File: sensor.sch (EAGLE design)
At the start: 30 parts, among them IC1 TP4056, U1 NX1117C33Z, U3 BMP180, U4 TSL2561, Y1 12mhz

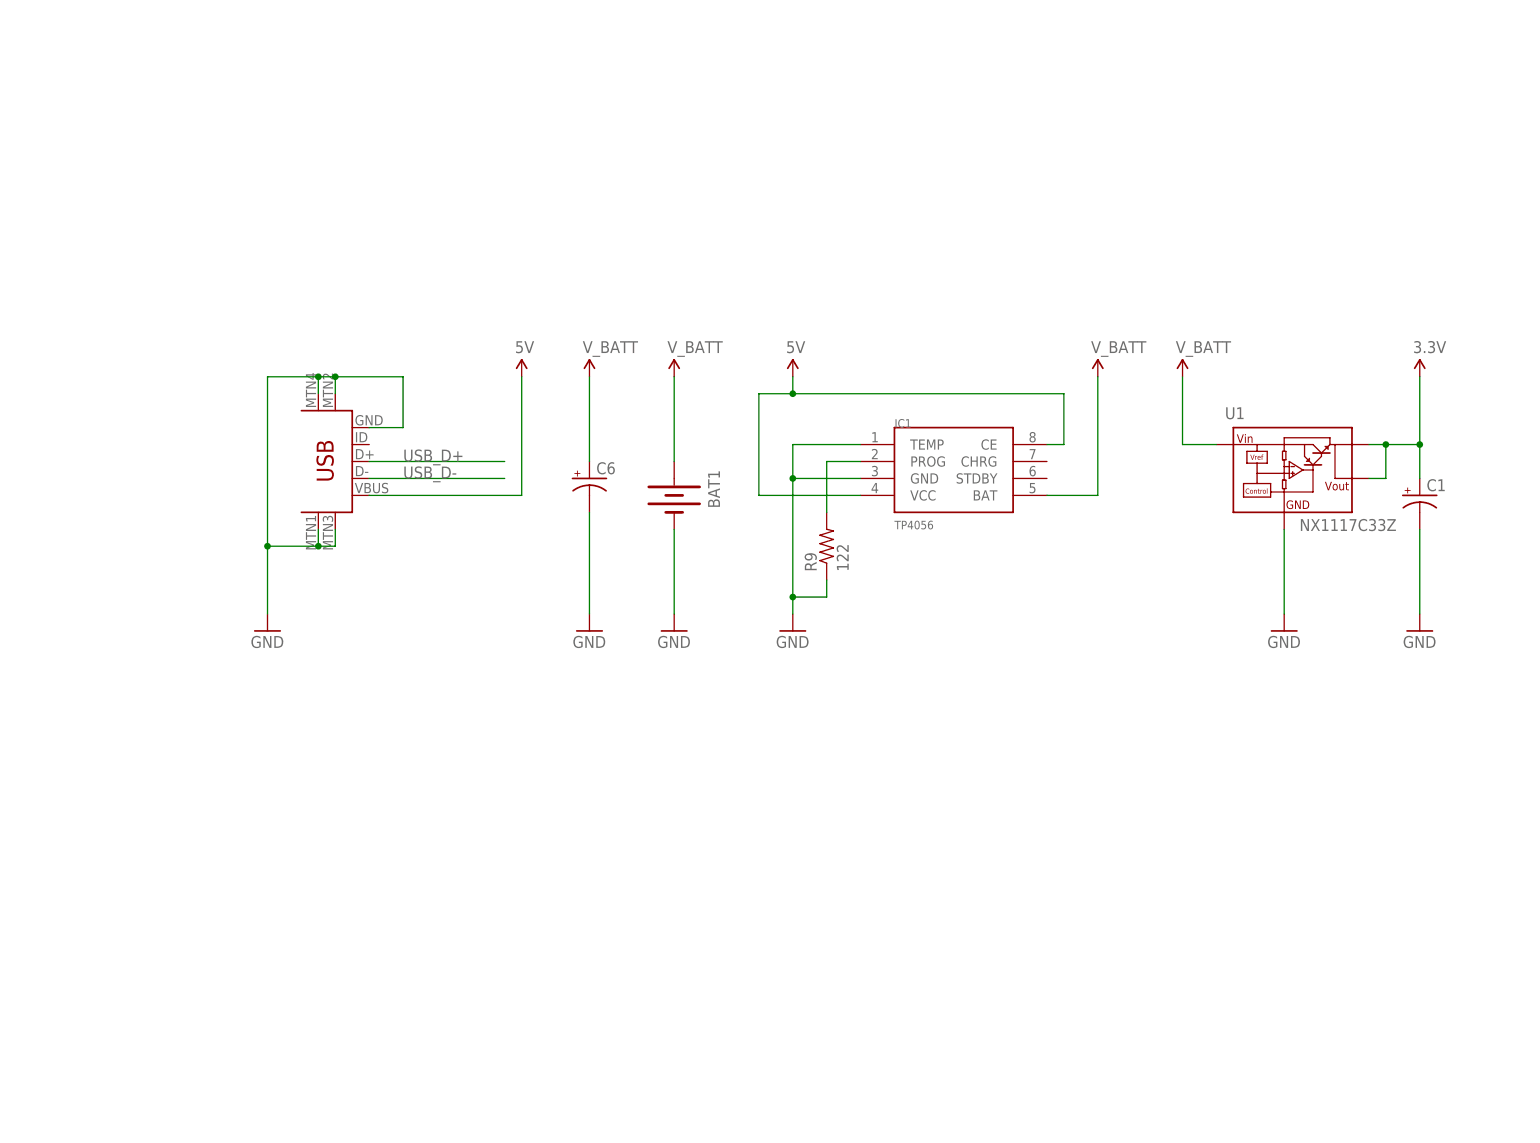
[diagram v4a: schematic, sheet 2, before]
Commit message: Moving to using MCP7381 and TPS63001.. Damn tiny ass packages.
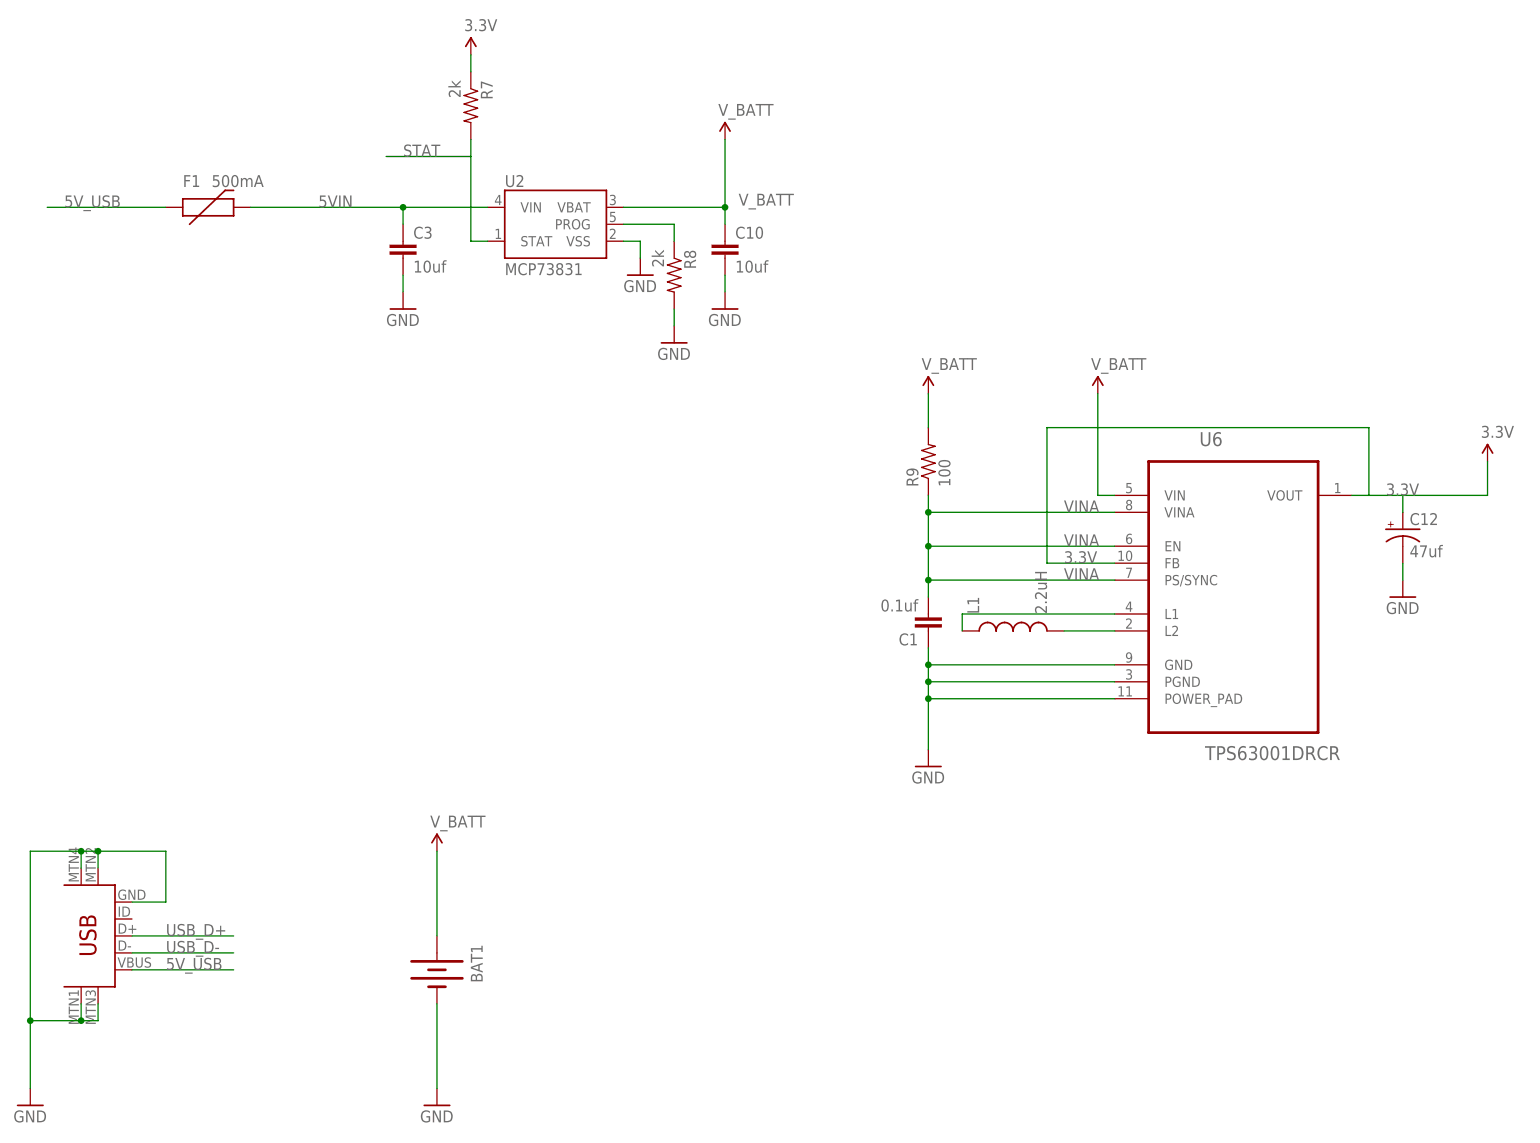
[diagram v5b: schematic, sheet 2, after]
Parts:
- removed C6: (no value), SparkFun-Capacitors:47UF-50V-20%(ELECT)
- removed IC1: TP4056, TP4056:TP4056
- removed U1: NX1117C33Z, nxp_60:NX1117C33Z
- added C10, C3: 10uf, SparkFun-Capacitors:CAP0805
- added C12: 47uf, SparkFun-Capacitors:CAP_POLC
- added EXP_I2C, EXP_UART: (no value), SparkFun-Connectors:M04LOCK
- added F1: 500mA, SparkFun:PTCSMD
- added L1: 2.2uH, SparkFun-Passives:INDUCTORSRU5028
- added R7, R8: 2k, SparkFun-Resistors:RESISTOR0805-RES
- added U2: MCP73831, SparkFun:MCP73831
- added U6: TPS63001DRCR, Texas Instruments_By_element14_Batch_1:TPS63001DRCR
- C1: value (none) -> 0.1uf; device SparkFun-Capacitors:47UF-50V-20%(ELECT) -> SparkFun-Capacitors:CAP0805
- R9: value 122 -> 100
- U$5: value ESP8266_ESP-12 -> (none); device ESP8266-ESP12:ESP8266_ESP-12 -> ESP8266-ESP12E:ESP8266-12EESP8266-ESP12E
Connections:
- net GPIO0 renamed SWITCH
- net GPIO14 renamed LED_R
- net GPIO2 renamed SENSE
- removed net 5V: IC1.CE, IC1.VCC, U$6.VBUS
- removed net GPIO12: LED2.BLU-A, U$5.GPIO12
- removed net GPIO13: U$5.GPIO13
- removed net GPIO16: LED2.GRN-A, U$5.GPIO16
- removed net N$3: IC1.PROG, R9.2
- new net 5VIN: C3.1, F1.2, U2.VIN
- new net 5V_USB: F1.1, U$6.VBUS
- new net LED_B: LED2.BLU-A, U$5.GPIO16
- new net LED_G: LED2.GRN-A, U$5.GPIO12
- new net N$1: L1.2, U6.L2
- new net N$11: R8.1, U2.PROG
- new net N$2: L1.1, U6.L1
- new net SOFT_RX: EXP_UART.2, U$5.GPIO10
- new net SOFT_TX: EXP_UART.1, U$5.GPIO9
- new net STAT: R7.2, U$5.GPIO13, U2.STAT
- new net VINA: C1.2, R9.1, U6.EN, U6.PS/SYNC, U6.VINA
- net 3.3V: now also C12.+, EXP_I2C.4, EXP_UART.4, R7.1, U6.FB, U6.VOUT; no longer C1.+, U1.VOUT, U1.VOUT1
- net GND: now also C1.1, C10.2, C12.-, C3.2, EXP_I2C.3, EXP_UART.3, R8.2, U2.VSS, U6.GND, U6.PGND, U6.POWER_PAD; no longer C1.-, C6.-, IC1.GND, IC1.TEMP, R9.1, U1.GND
- net SCL: now also EXP_I2C.1, U$5.GPIO4; no longer U$5.GPIO5
- net SDA: now also EXP_I2C.2, U$5.GPIO5; no longer U$5.GPIO4
- net V_BATT: now also C10.1, R9.2, U2.VBAT, U6.VIN; no longer C6.+, IC1.BAT, U1.VIN
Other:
- moved on the sheet: BAT1, R9

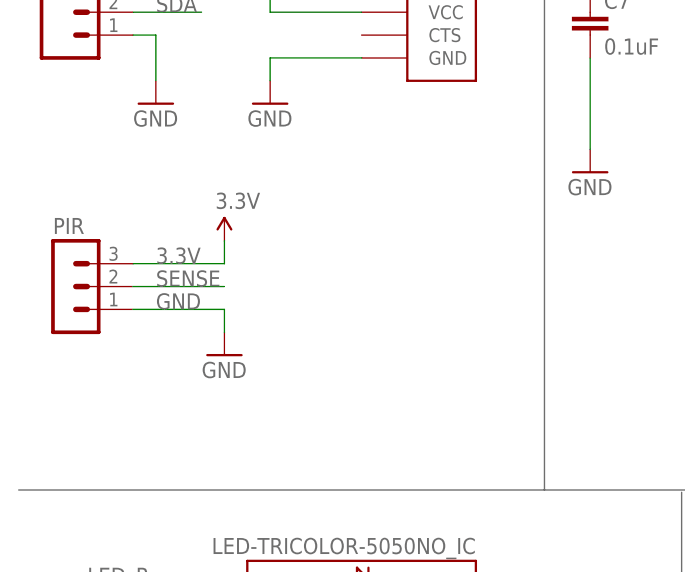
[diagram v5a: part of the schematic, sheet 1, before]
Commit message: Tart the PCB up a bit, nice 45 degree bends. Add a 0.1uf cap across the PIR sensor.
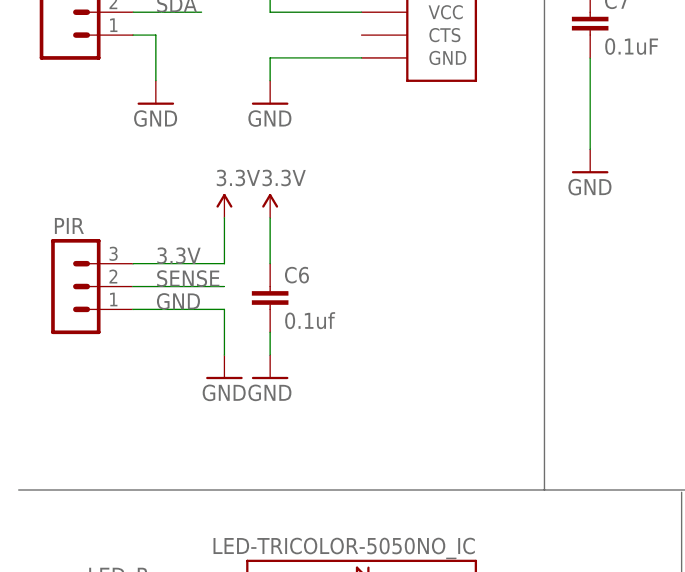
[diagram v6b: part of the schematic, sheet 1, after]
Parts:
- added C6: 0.1uf, SparkFun-Capacitors:CAP0805
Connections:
- net 3.3V: now also C6.1
- net GND: now also C6.2
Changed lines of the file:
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@@
 <part name="EXP_UART" library="SparkFun-Connectors" deviceset="M04" device="LOCK"/>
 <part name="EXP_I2C" library="SparkFun-Connectors" deviceset="M04" device="LOCK"/>
+<part name="C6" library="SparkFun-Capacitors" deviceset="CAP" device="0805" value="0.1uf"/>
+<part name="SUPPLY18" library="SparkFun-Aesthetics" deviceset="3.3V" device=""/>
+<part name="GND11" library="SparkFun" deviceset="GND" device=""/>
 </parts>
 <sheets>
@@
 <instance part="LOGO1" gate="G$1" x="165.1" y="12.7"/>
 <instance part="PIR" gate="G$1" x="5.08" y="58.42"/>
-<instance part="GND4" gate="1" x="22.86" y="50.8"/>
+<instance part="GND4" gate="1" x="22.86" y="48.26"/>
 <instance part="JP2" gate="G$1" x="43.18" y="91.44"/>
 <instance part="S1" gate="G$1" x="109.22" y="12.7"/>
@@
 <instance part="Y1" gate="G$1" x="96.52" y="60.96"/>
 <instance part="SUPPLY4" gate="G$1" x="15.24" y="99.06"/>
-<instance part="SUPPLY17" gate="G$1" x="22.86" y="63.5"/>
+<instance part="SUPPLY17" gate="G$1" x="22.86" y="66.04"/>
 <instance part="LED2" gate="D1" x="38.1" y="22.86" rot="R180"/>
 <instance part="GND1" gate="1" x="63.5" y="12.7"/>
@@
 <instance part="EXP_UART" gate="G$1" x="157.48" y="88.9"/>
 <instance part="EXP_I2C" gate="G$1" x="157.48" y="71.12"/>
+<instance part="C6" gate="G$1" x="27.94" y="55.88"/>
+<instance part="SUPPLY18" gate="G$1" x="27.94" y="66.04"/>
+<instance part="GND11" gate="1" x="27.94" y="48.26"/>
 </instances>
 <busses>
@@
 <pinref part="PIR" gate="G$1" pin="3"/>
 <wire x1="22.86" y1="60.96" x2="12.7" y2="60.96" width="0.1524" layer="91"/>
-<wire x1="22.86" y1="60.96" x2="22.86" y2="63.5" width="0.1524" layer="91"/>
+<wire x1="22.86" y1="60.96" x2="22.86" y2="66.04" width="0.1524" layer="91"/>
 <label x="15.24" y="60.96" size="1.778" layer="95"/>
 <pinref part="SUPPLY17" gate="G$1" pin="3.3V"/>
@@
 <wire x1="162.56" y1="76.2" x2="180.34" y2="76.2" width="0.1524" layer="91"/>
 <label x="165.1" y="76.2" size="1.778" layer="95"/>
+</segment>
+<segment>
+<pinref part="C6" gate="G$1" pin="1"/>
+<pinref part="SUPPLY18" gate="G$1" pin="3.3V"/>
+<wire x1="27.94" y1="60.96" x2="27.94" y2="66.04" width="0.1524" layer="91"/>
 </segment>
 </net>
@@
 <wire x1="12.7" y1="55.88" x2="22.86" y2="55.88" width="0.1524" layer="91"/>
 <pinref part="GND4" gate="1" pin="GND"/>
-<wire x1="22.86" y1="55.88" x2="22.86" y2="53.34" width="0.1524" layer="91"/>
+<wire x1="22.86" y1="55.88" x2="22.86" y2="50.8" width="0.1524" layer="91"/>
 <label x="15.24" y="55.88" size="1.778" layer="95"/>
 </segment>
@@
 <label x="165.1" y="73.66" size="1.778" layer="95"/>
 </segment>
+<segment>
+<pinref part="C6" gate="G$1" pin="2"/>
+<pinref part="GND11" gate="1" pin="GND"/>
+<wire x1="27.94" y1="53.34" x2="27.94" y2="50.8" width="0.1524" layer="91"/>
+</segment>
 </net>
